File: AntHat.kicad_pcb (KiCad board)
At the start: 4 copper layers, 65 x 56.5 mm, 62 parts, among them J1 Raspberry_Pi_2_3, J10 0353180420, J11 0353180420, J2 0455580003, J3 PSU Comm, J4 61900411021, J5 61900411021, J6 61900411021, J7 61900411021, J8 0353180420, J9 0353180420, Q1 DMP3013SFV-7, U1 AP64501SP-13, U2 EMC2305

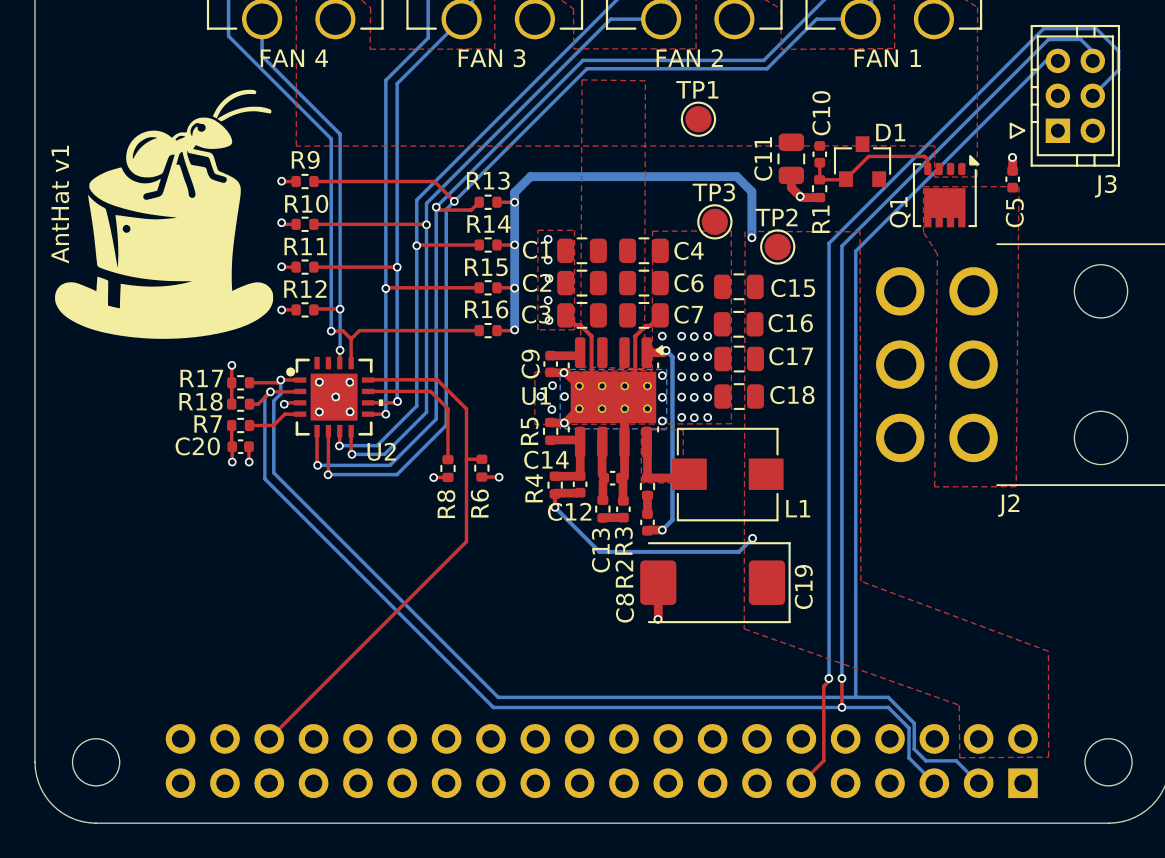
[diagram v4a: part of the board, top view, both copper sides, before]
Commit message: add fix for #1
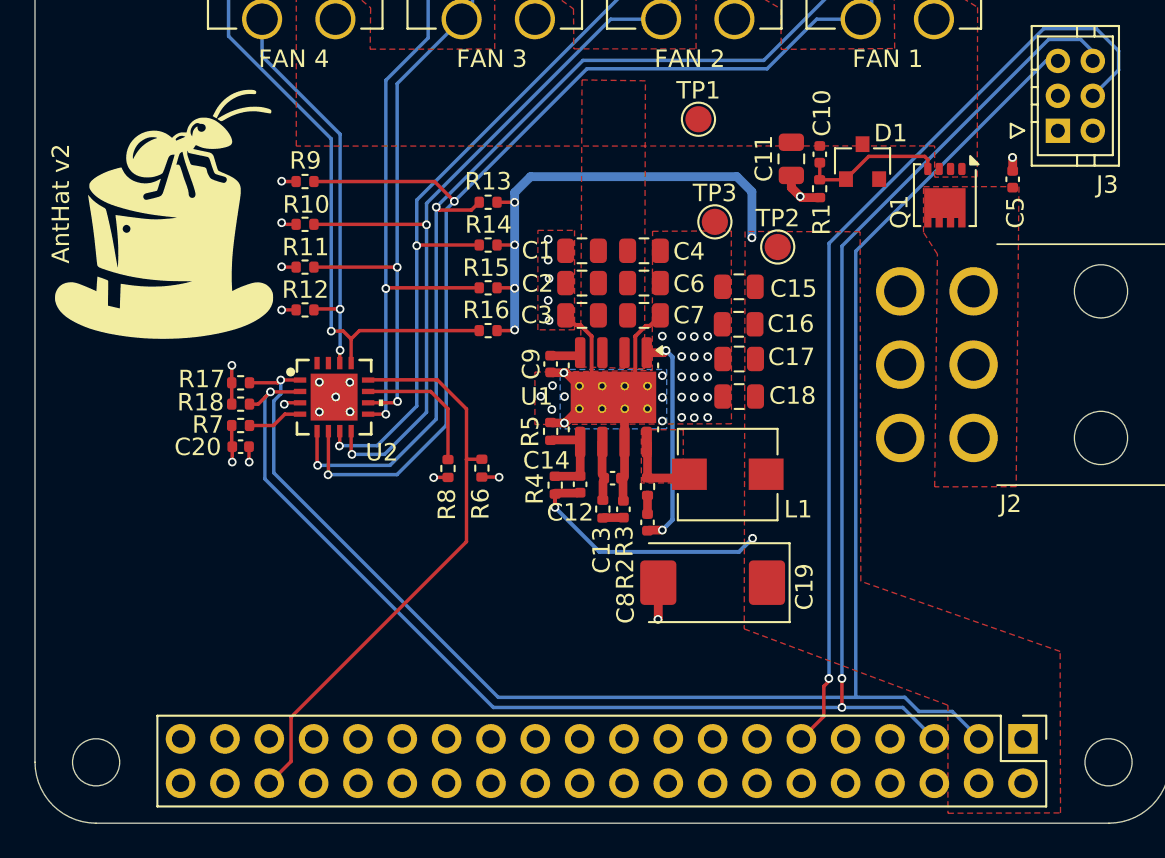
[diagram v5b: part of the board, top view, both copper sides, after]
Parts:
- J1: moved to F.Cu
- moved J1 2.54 mm to (163.7, 121.0), turned to -90 degrees
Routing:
- net /PSU_EN: track 57.0 -> 54.4 mm
- net /FAN_ALERT: track 30.8 -> 33.3 mm
- net /SCL: track 101.4 -> 99.4 mm
- net /SDA: track 98.7 -> 96.8 mm
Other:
- board text added: "AntHat v2"
- board text removed: "AntHat v1"

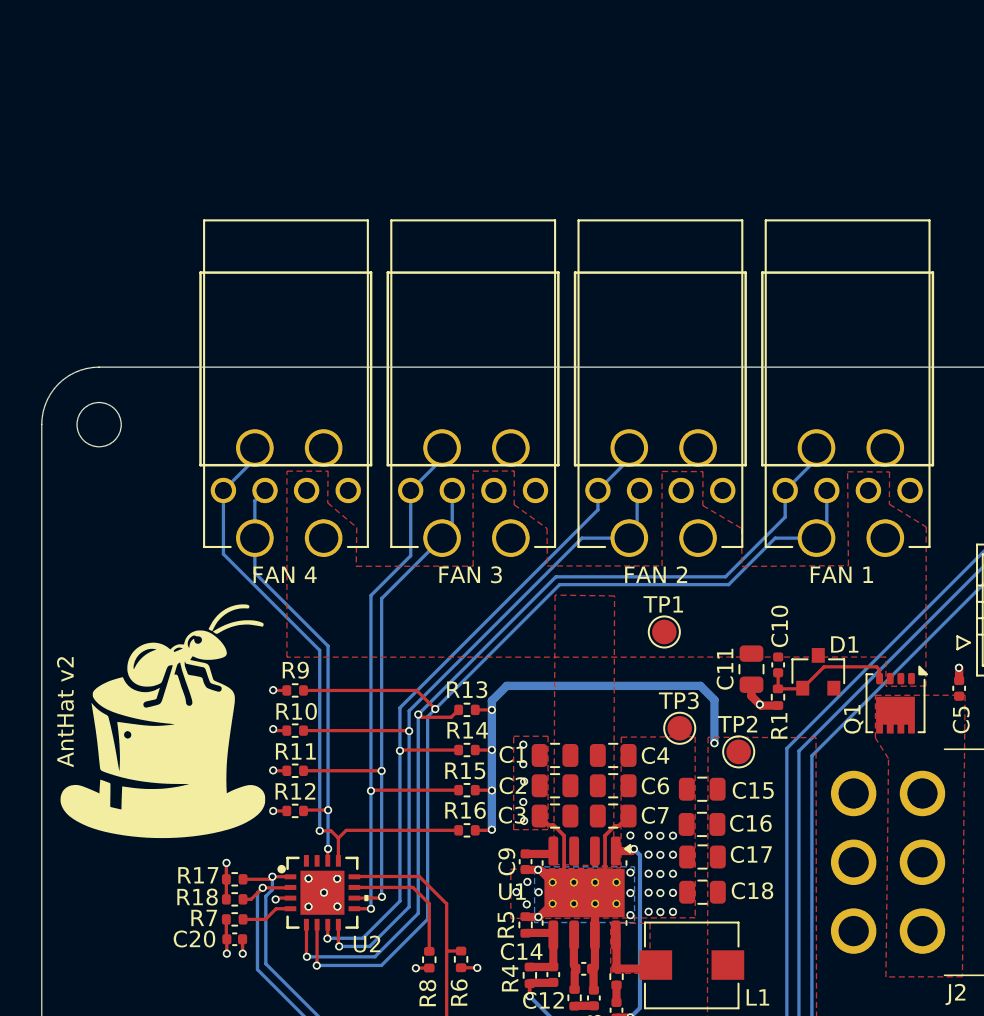
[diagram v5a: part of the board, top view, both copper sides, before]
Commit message: started to add TPS259241
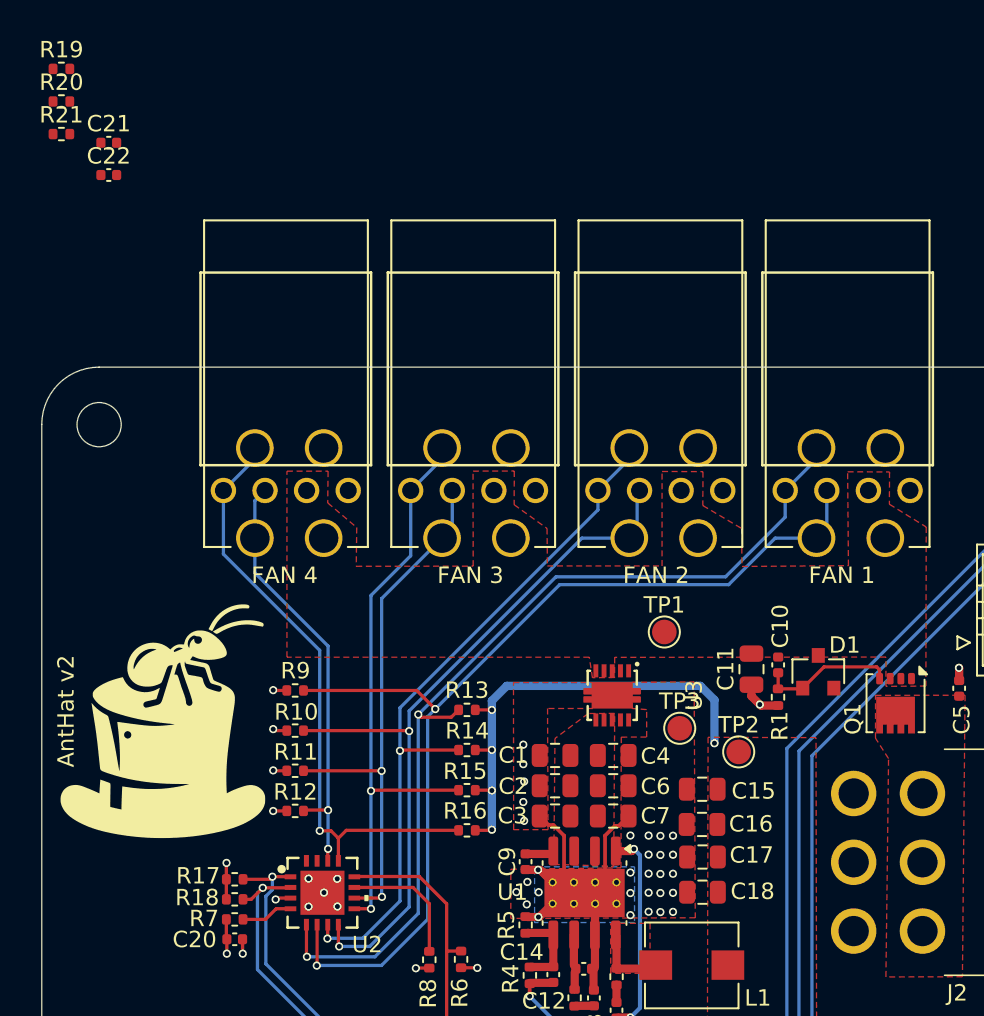
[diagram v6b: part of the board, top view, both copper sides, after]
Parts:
- added C21: 1200pF, Capacitor_SMD:C_0402_1005Metric, F.Cu at (111.2, 55.6)
- added C22: 1200pF, Capacitor_SMD:C_0402_1005Metric, F.Cu at (111.2, 57.6)
- added R19: 2.2k, Resistor_SMD:R_0402_1005Metric, F.Cu at (108.3, 51.1)
- added R20: 2.2k, Resistor_SMD:R_0402_1005Metric, F.Cu at (108.3, 53.1)
- added R21: 2.2k, Resistor_SMD:R_0402_1005Metric, F.Cu at (108.3, 55.1)
- added U3: TPS259241DRCR, AntHat:VSON-10_L3.0-W3.0-P0.50-TL-EP, F.Cu at (142.0, 89.3)
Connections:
- C1 pad 1: /12V -> /12V_LIM
- C2 pad 1: /12V -> /12V_LIM
- C3 pad 1: /12V -> /12V_LIM
- C4 pad 1: /12V -> /12V_LIM
- C6 pad 1: /12V -> /12V_LIM
- C7 pad 1: /12V -> /12V_LIM
- U1 pad 2: /12V -> /12V_LIM
- U1 pad 3: /12V -> /12V_LIM
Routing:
- added copper zone on F.Cu, net /12V_LIM

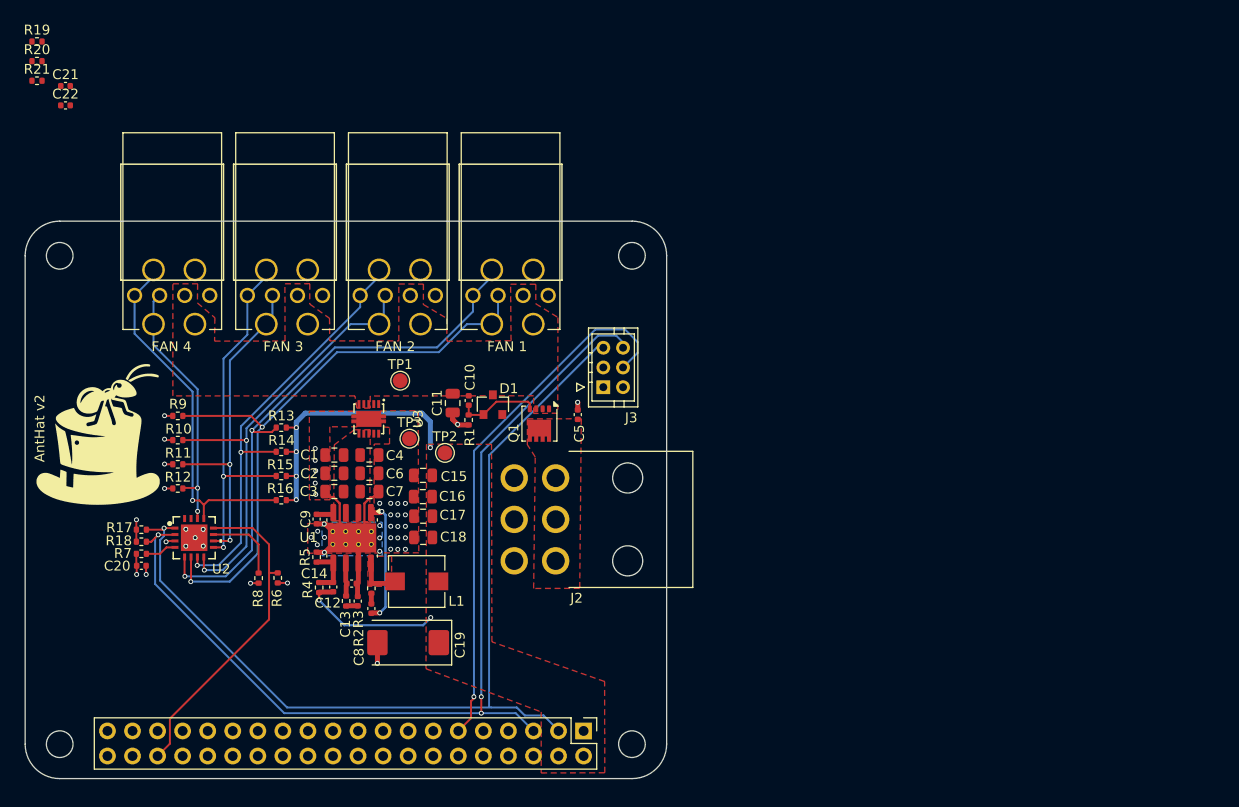
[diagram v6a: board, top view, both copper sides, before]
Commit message: combined the fan connector styles. added some LCSC part numbers. switched PSU I2C over to GPIO for bit banging.
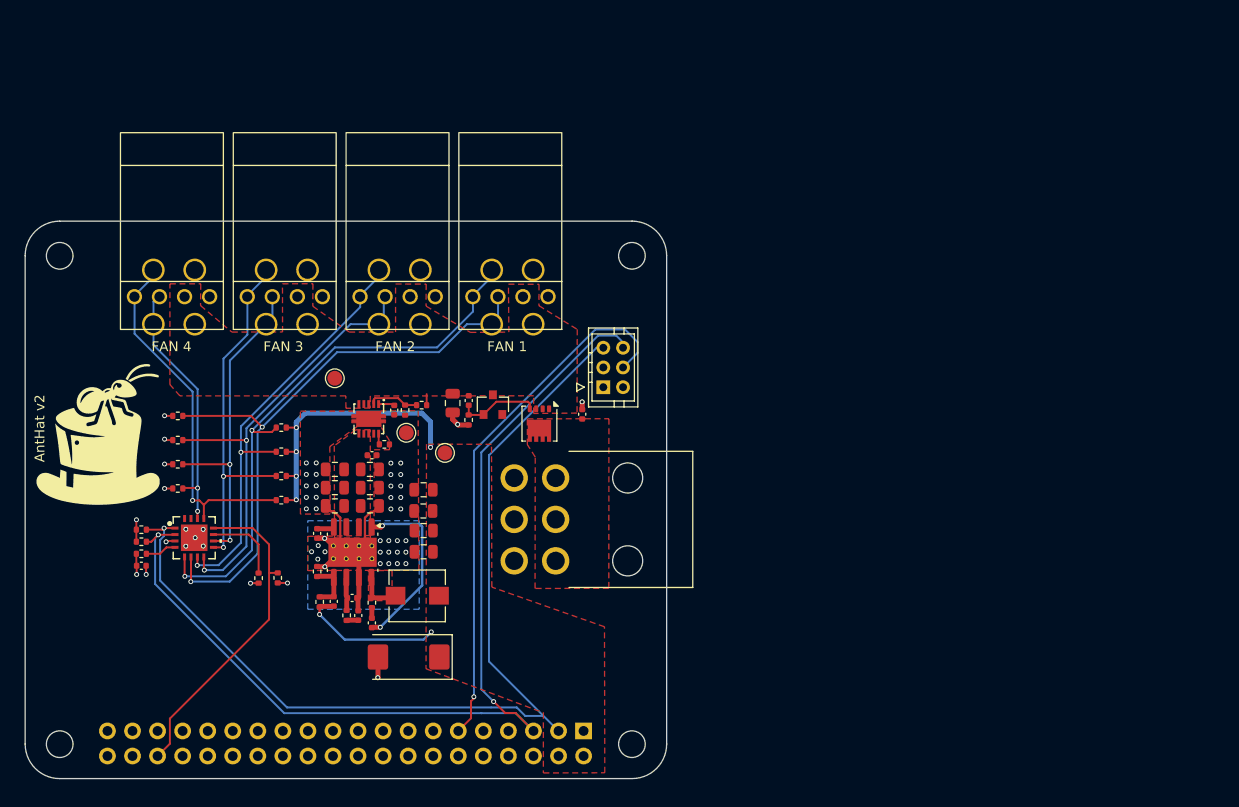
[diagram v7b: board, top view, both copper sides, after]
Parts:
- removed J10, J11, J8, J9: 0353180420, AntHat:MOLEX_353180420
- J4, J5: footprint AntHat:CONN_61900411021_WRE -> AntHat:MOLEX_1x4_2x2_combo
- J6, J7: value 61900411021 -> 0353180420; footprint AntHat:CONN_61900411021_WRE -> AntHat:MOLEX_1x4_2x2_combo
- moved R19 53.7 mm to (147.3, 88.0), turned to 180 degrees
- moved R20 51.4 mm to (145.7, 88.5), turned to -90 degrees
- moved R21 51.0 mm to (143.6, 91.9)
- moved C22 47.1 mm to (142.3, 93.0)
- moved C21 46.8 mm to (144.6, 88.5), turned to -90 degrees
- moved TP1 6.63 mm to (138.5, 85.2), turned to 180 degrees
- moved J4 6.28 mm to (154.4, 74.2)
- moved J5 6.28 mm to (143.0, 74.2)
- moved J6 6.28 mm to (131.6, 74.2)
- moved J7 6.28 mm to (120.1, 74.2)
- moved C17 1.46 mm to (147.5, 100.7)
- moved C3 1.46 mm to (138.5, 98.2)
- moved C7 1.46 mm to (142.1, 98.2)
- moved C15 1.46 mm to (147.5, 96.5)
- moved C1 1.46 mm to (138.5, 94.5)
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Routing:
- net Net-(U1-BST): track 12.6 -> 18.1 mm
- net Net-(U3-EN/UVLO): track 0.00 -> 5.15 mm
- net /SCL: track 99.4 -> 104.0 mm, vias 3 -> 2
- net /SDA: track 96.8 -> 99.9 mm
- net Net-(U3-dV/dT): track 0.00 -> 1.63 mm
- net /12V: track 0.00 -> 1.12 mm
- net Net-(U3-ILIM): track 0.00 -> 1.11 mm
- net GND: vias 39 -> 47

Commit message: add inductor 3d model. update render
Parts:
- added R22: 4.7k, Resistor_SMD:R_0402_1005Metric, F.Cu at (149.8, 116.9)
- added R23: 4.7k, Resistor_SMD:R_0402_1005Metric, F.Cu at (145.8, 116.9)
- moved TP1 9.28 mm to (147.8, 85.6)
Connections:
- J1 pad 13: unconnected-(J1-GPIO27-Pad13) -> /PSU_SCL
- J1 pad 15: unconnected-(J1-GPIO22-Pad15) -> /PSU_SDA
- J3 pad 3: /SDA -> /PSU_SDA
- J3 pad 6: /SCL -> /PSU_SCL
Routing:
- net /PSU_SDA: track 0.00 -> 53.9 mm, vias 0 -> 1
- net /PSU_SCL: track 0.00 -> 53.1 mm, vias 0 -> 1
- net /SCL: track 104.0 -> 52.8 mm, vias 2 -> 1
- net /SDA: track 99.9 -> 55.2 mm
- net /3V3: track 10.5 -> 12.1 mm, vias 9 -> 11
- net GND: track 23.6 -> 23.0 mm
